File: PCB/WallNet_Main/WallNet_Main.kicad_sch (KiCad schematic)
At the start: 27 parts, among them J1 Conn_01x05_Pin, J2 USB_C_Receptacle_PowerOnly_6P, J3 Conn_01x04_Pin, J4 Conn_01x04_Pin, SW1 SW, SW2 SW, U1 NRF52810-QCAA-R7, U2 CPT-9019B-SMT-TR, U3 BQ25895RTWT, Y1 ECS-320-8-37CKM

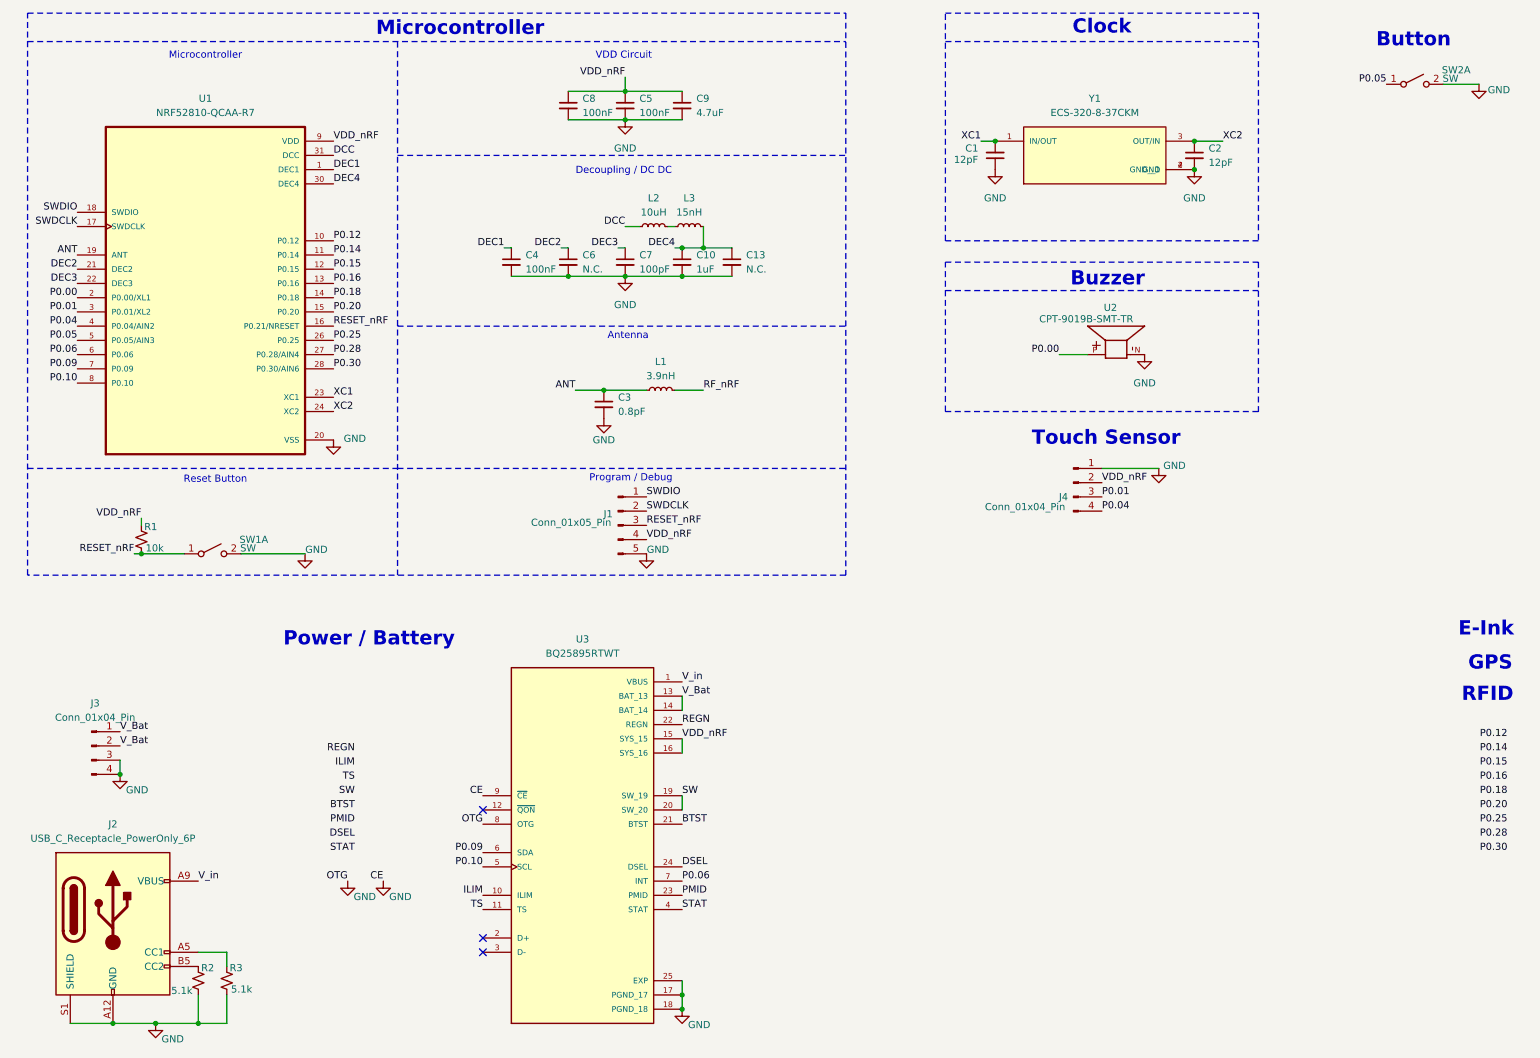
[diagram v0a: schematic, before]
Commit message: Changed Microcontroller
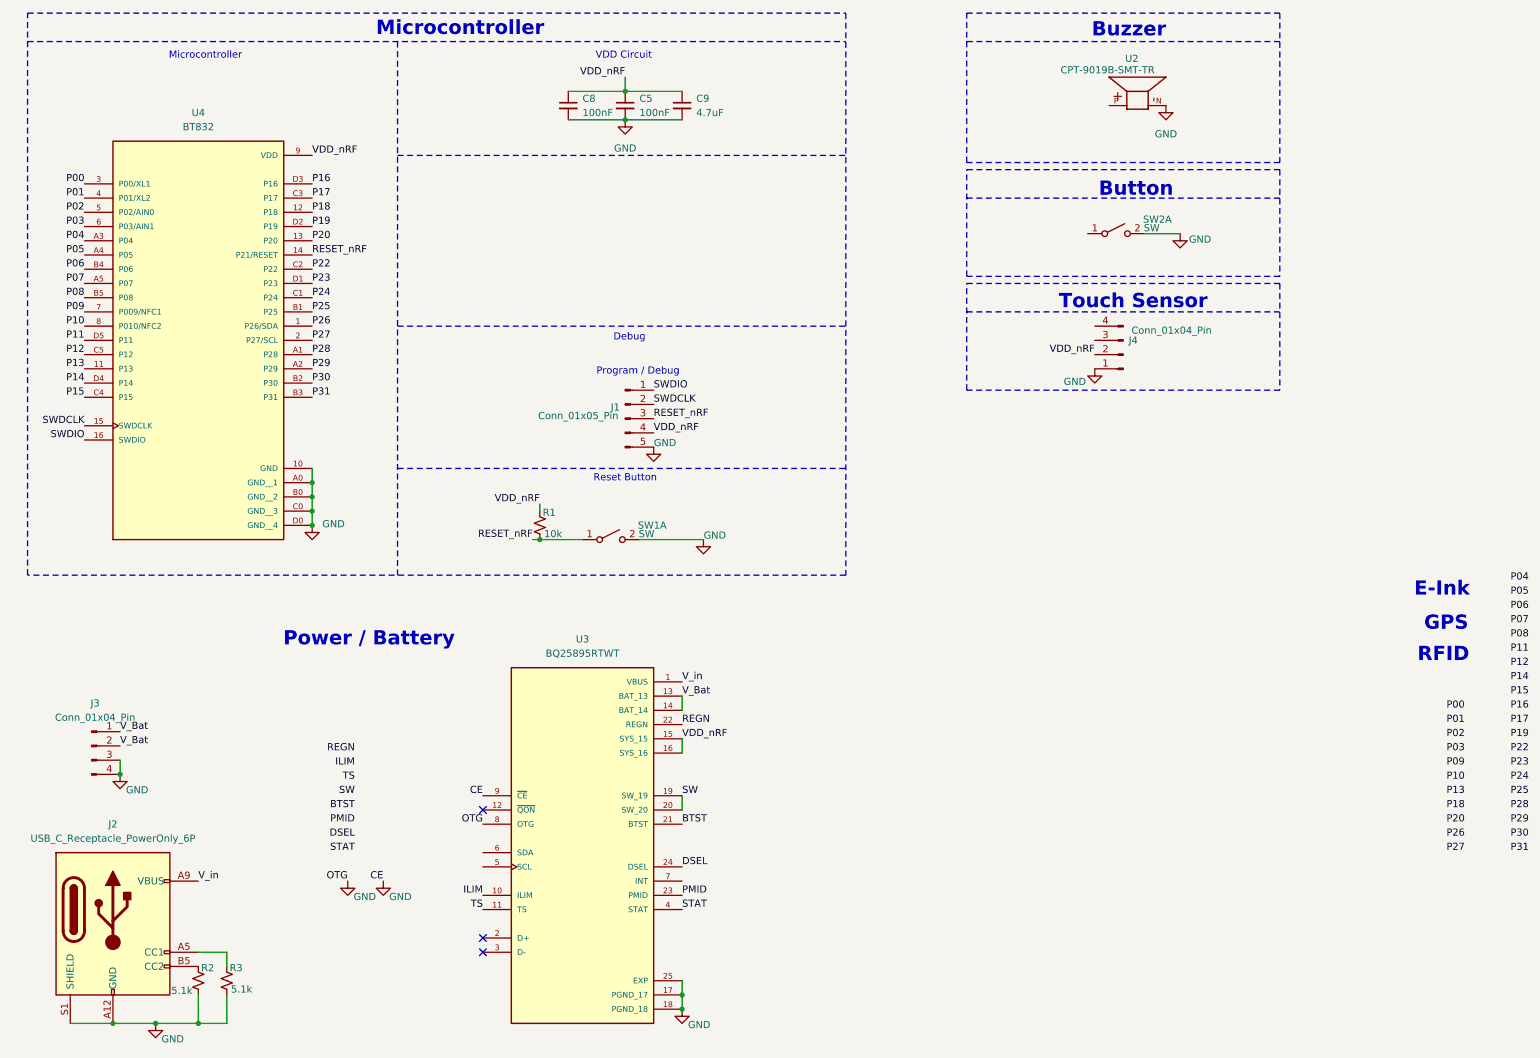
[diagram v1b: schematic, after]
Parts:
- removed C1, C2: 12pF, Capacitor_SMD:C_0402_1005Metric, symbol Device:C_Small
- removed C10: 1uF, Capacitor_SMD:C_0201_0603Metric, symbol Device:C_Small
- removed C13, C6: N.C., Capacitor_SMD:C_0402_1005Metric, symbol Device:C_Small
- removed C3: 0.8pF, Capacitor_SMD:C_0402_1005Metric, symbol Device:C_Small
- removed C4: 100nF, Capacitor_SMD:C_0402_1005Metric, symbol Device:C_Small
- removed C7: 100pF, Capacitor_SMD:C_0402_1005Metric, symbol Device:C_Small
- removed L1: 3.9nH, Inductor_SMD:L_0402_1005Metric, symbol Device:L_Small
- removed L2: 10uH, Inductor_SMD:L_0201_0603Metric, symbol Device:L_Small
- removed L3: 15nH, Inductor_SMD:L_0402_1005Metric, symbol Device:L_Small
- removed U1: NRF52810-QCAA-R7, NRF52810-QCAA-R7:QFN50P500X500X90-33N, symbol NRF52810-QCAA-R7:NRF52810-QCAA-R7
- removed Y1: ECS-320-8-37CKM, ECS_320_8_37CKM:XTAL_ECS-320-8-37CKM, symbol ECS-320-8-37CKM:ECS-320-8-37CKM
- added U4: BT832, BT832:BLEMODULE_BT832, symbol BT832:BT832
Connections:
- net GND: now also U4.10 (GND), U4.A0 (GND__1), U4.B0 (GND__2), U4.C0 (GND__3), U4.D0 (GND__4)
- net RESET_nRF: now also U4.14 (P21/RESET)
- net SWDCLK: now also U4.15 (SWDCLK)
- net SWDIO: now also U4.16 (SWDIO)
- net P0.00: no longer names the net of U2.P
- net P0.01: no longer names the net of J4.3 (Pin_3)
- net P0.04: no longer names the net of J4.4 (Pin_4)
- net P0.05: no longer names the net of SW2.1 (A)
- net P0.06: no longer names the net of U3.7 (INT)
- net P0.09: no longer names the net of U3.6 (SDA)
- net P0.10: no longer names the net of U3.5 (SCL)
- net VDD renamed VDD_nRF
- net VDD_nRF: now also U4.9 (VDD)
- new net P00: U4.3 (P00/XL1)
- new net P01: U4.4 (P01/XL2)
- new net P02: U4.5 (P02/AIN0)
- new net P03: U4.6 (P03/AIN1)
- new net P04: U4.A3 (P04)
- new net P05: U4.A4 (P05)
- new net P06: U4.B4 (P06)
- new net P07: U4.A5 (P07)
- new net P08: U4.B5 (P08)
- new net P09: U4.7 (P009/NFC1)
- new net P10: U4.8 (P010/NFC2)
- new net P11: U4.D5 (P11)
- new net P12: U4.C5 (P12)
- new net P13: U4.11 (P13)
- new net P14: U4.D4 (P14)
- new net P15: U4.C4 (P15)
- new net P16: U4.D3 (P16)
- new net P17: U4.C3 (P17)
- new net P18: U4.12 (P18)
- new net P19: U4.D2 (P19)
- new net P20: U4.13 (P20)
- new net P22: U4.C2 (P22)
- new net P23: U4.D1 (P23)
- new net P24: U4.C1 (P24)
- new net P25: U4.B1 (P25)
- new net P26: U4.1 (P26/SDA)
- new net P27: U4.2 (P27/SCL)
- new net P28: U4.A1 (P28)
- new net P29: U4.A2 (P29)
- new net P30: U4.B2 (P30)
- new net P31: U4.B3 (P31)
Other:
- note added: "Debug"
- note removed: "Antenna"
- note removed: "Clock"
- note removed: "Decoupling / DC DC"
- moved on the sheet: J1, J4, R1, SW1A, SW2A, U2

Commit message: Power Management Finished
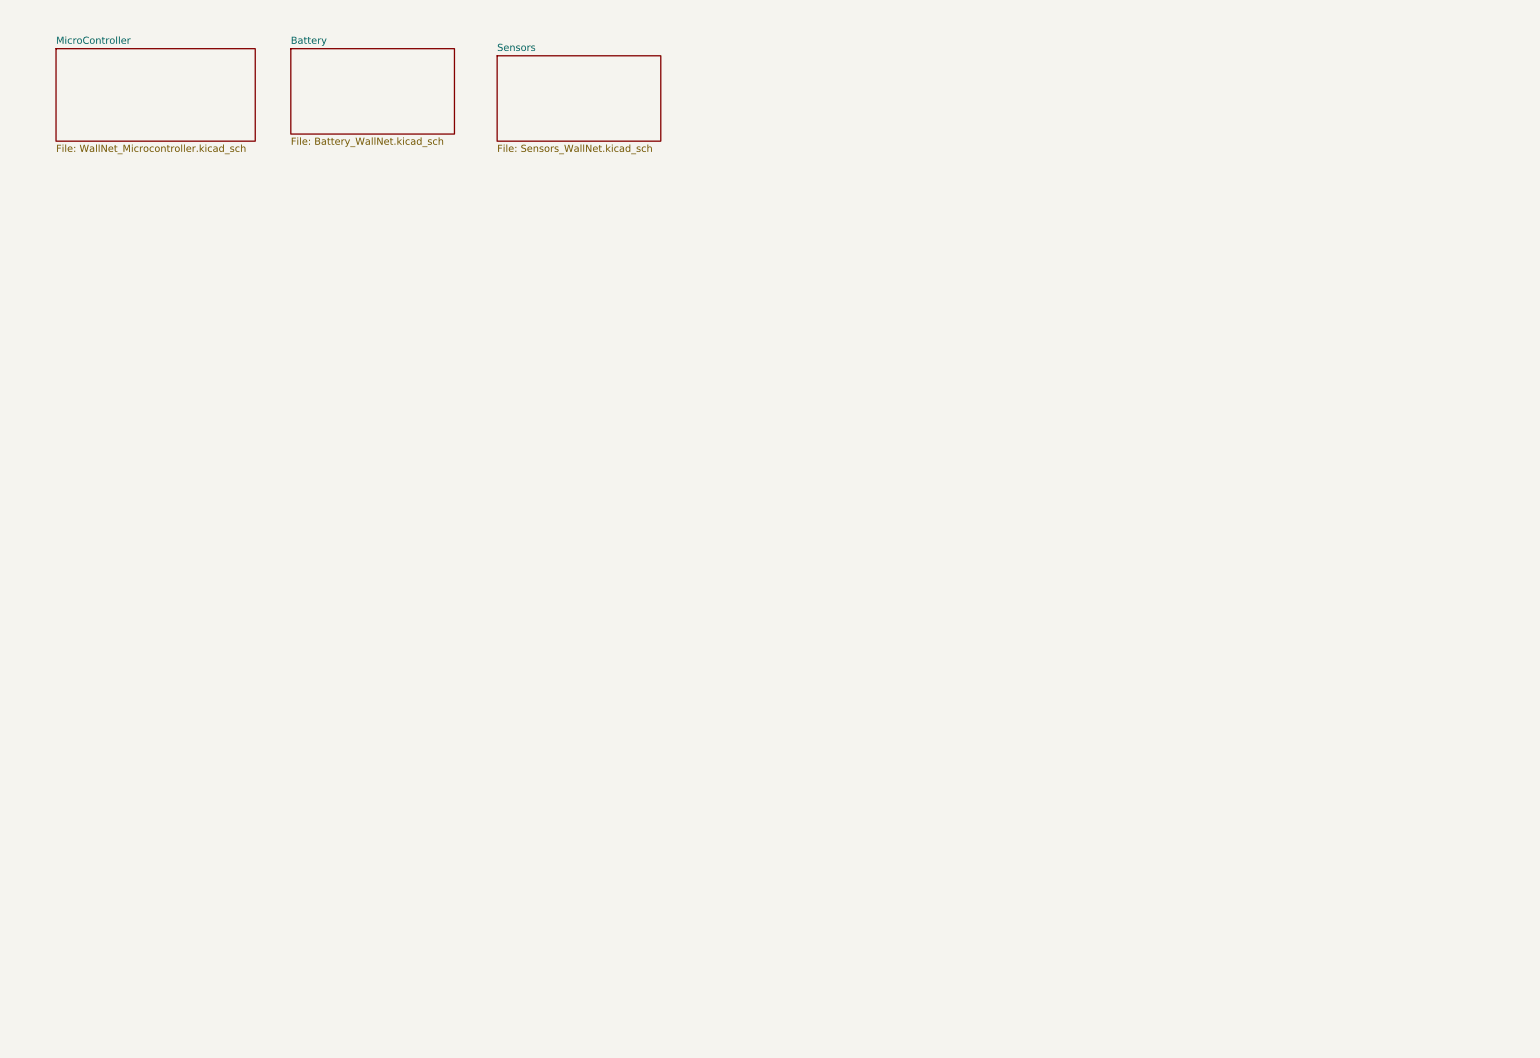
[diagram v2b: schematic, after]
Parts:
- removed C5, C8: 100nF, Capacitor_SMD:C_0402_1005Metric, symbol Device:C_Small
- removed C9: 4.7uF, Capacitor_SMD:C_0201_0603Metric, symbol Device:C_Small
- removed J1: Conn_01x05_Pin, Connector_PinHeader_2.54mm:PinHeader_1x05_P2.54mm_Vertical, symbol Connector:Conn_01x05_Pin
- removed J2: USB_C_Receptacle_PowerOnly_6P, symbol Connector:USB_C_Receptacle_PowerOnly_6P
- removed J3, J4: Conn_01x04_Pin, Connector_Molex:Molex_CLIK-Mate_502494-0470_1x04-1MP_P2.00mm_Horizontal, symbol Connector:Conn_01x04_Pin
- removed R1: 10k, Resistor_SMD:R_0201_0603Metric, symbol Device:R_Small_US
- removed R2, R3: 5.1k, Resistor_SMD:R_0201_0603Metric, symbol Device:R_Small_US
- removed SW1, SW2: SW, symbol Switch:SW_DPST_x2
- removed U2: CPT-9019B-SMT-TR, CPT_9019B_SMT_TR:XDCR_CPT-9019B-SMT-TR, symbol CPT-9019B-SMT-TR:CPT-9019B-SMT-TR
- removed U3: BQ25895RTWT, Package_DFN_QFN:Texas_RTW_WQFN-24-1EP_4x4mm_P0.5mm_EP2.7x2.7mm, symbol BQ25895RTWT:BQ25895RTWT
- removed U4: BT832, BT832:BLEMODULE_BT832, symbol BT832:BT832
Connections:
- no-connect marks 3 -> 0
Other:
- added sheet Battery (Battery_WallNet.kicad_sch)
- added sheet MicroController (WallNet_Microcontroller.kicad_sch)
- added sheet Sensors (Sensors_WallNet.kicad_sch)
- note removed: "Button"
- note removed: "Buzzer"
- note removed: "Debug"
- note removed: "E-Ink"
- note removed: "GPS"
- note removed: "Microcontroller"
- note removed: "Power / Battery"
- note removed: "Program / Debug"
- note removed: "RFID"
- note removed: "Reset Button"
- note removed: "Touch Sensor"
- note removed: "VDD Circuit"

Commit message: bruh
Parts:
- added C1, C2: 100nF, Capacitor_SMD:C_0402_1005Metric, symbol Device:C_Small
- added C3: 4.7uF, Capacitor_SMD:C_0201_0603Metric, symbol Device:C_Small
- added J1: Conn_01x05_Pin, Connector_PinHeader_2.54mm:PinHeader_1x05_P2.54mm_Vertical, symbol Connector:Conn_01x05_Pin
- added R1: 10k, symbol Device:R_Small_US
- added SW1: SW, symbol Switch:SW_DPST_x2
- added U4: BT832, BT832:BLEMODULE_BT832, symbol BT832:BT832
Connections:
- new net GND: C1.2, C2.2, C3.2, J1.5 (Pin_5), SW1.2 (B), U4.10 (GND), U4.A0 (GND__1), U4.B0 (GND__2), U4.C0 (GND__3), U4.D0 (GND__4)
- new net P00: U4.3 (P00/XL1)
- new net P01: U4.4 (P01/XL2)
- new net P02: U4.5 (P02/AIN0)
- new net P03: U4.6 (P03/AIN1)
- new net P04: U4.A3 (P04)
- new net P05: U4.A4 (P05)
- new net P06: U4.B4 (P06)
- new net P07: U4.A5 (P07)
- new net P08: U4.B5 (P08)
- new net P09: U4.7 (P009/NFC1)
- new net P10: U4.8 (P010/NFC2)
- new net P11: U4.D5 (P11)
- new net P12: U4.C5 (P12)
- new net P13: U4.11 (P13)
- new net P14: U4.D4 (P14)
- new net P15: U4.C4 (P15)
- new net P16: U4.D3 (P16)
- new net P17: U4.C3 (P17)
- new net P18: U4.12 (P18)
- new net P19: U4.D2 (P19)
- new net P20: U4.13 (P20)
- new net P22: U4.C2 (P22)
- new net P23: U4.D1 (P23)
- new net P24: U4.C1 (P24)
- new net P25: U4.B1 (P25)
- new net P26: U4.1 (P26/SDA)
- new net P27: U4.2 (P27/SCL)
- new net P28: U4.A1 (P28)
- new net P29: U4.A2 (P29)
- new net P30: U4.B2 (P30)
- new net P31: U4.B3 (P31)
- new net RESET_nRF: J1.3 (Pin_3), R1.2, SW1.1 (A), U4.14 (P21/RESET)
- new net SWDCLK: J1.2 (Pin_2), U4.15 (SWDCLK)
- new net SWDIO: J1.1 (Pin_1), U4.16 (SWDIO)
- new net VDD_nRF: C1.1, C2.1, C3.1, J1.4 (Pin_4)
- new net VDD_nrf: R1.1, U4.9 (VDD)
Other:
- removed sheet MicroController
- sheet Battery ports: added BQ_INT, BQ_SCL, BQ_SDA; removed none
- note added: "Debug"
- note added: "Microcontroller"
- note added: "Program / Debug"
- note added: "Reset Button"
- note added: "VDD Circuit"

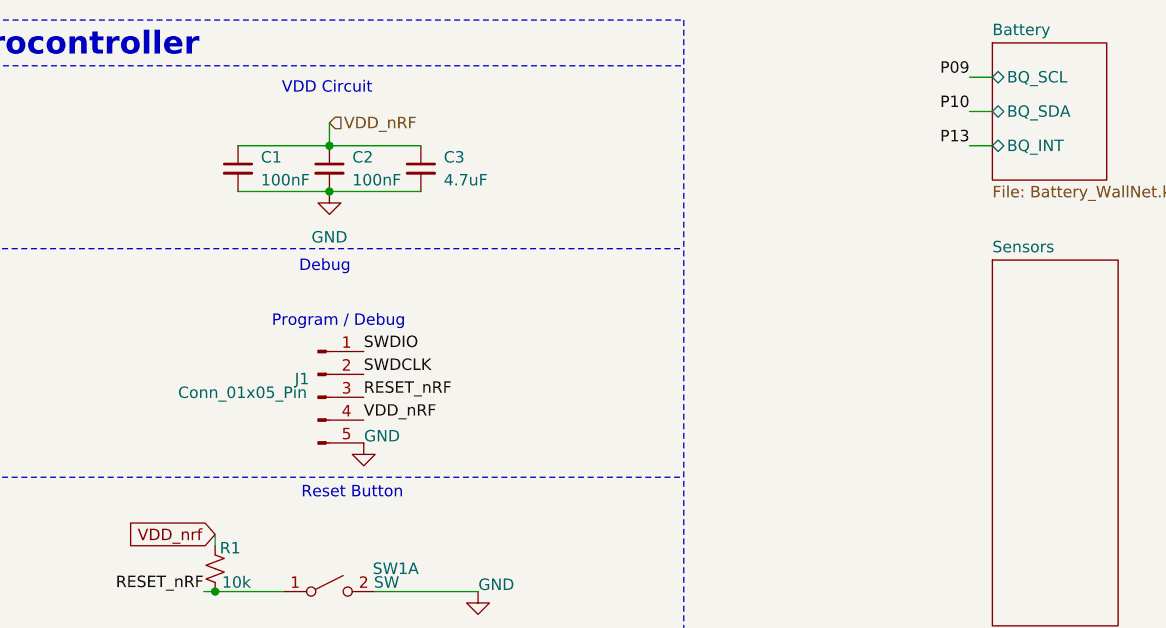
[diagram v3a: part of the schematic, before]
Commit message: Changed some Heir connections
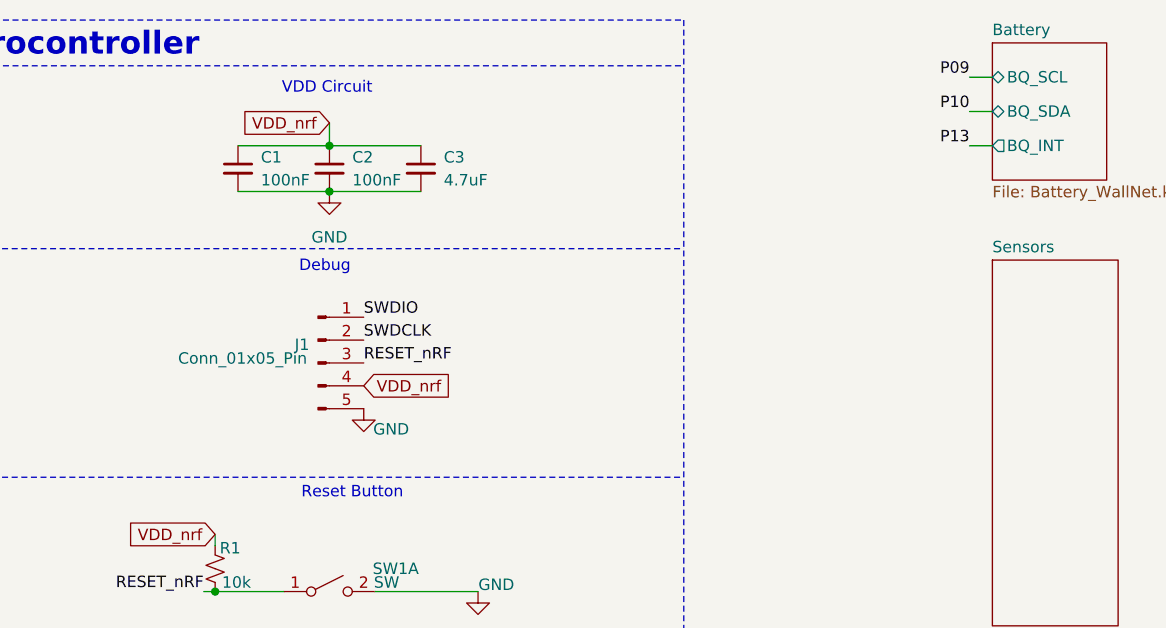
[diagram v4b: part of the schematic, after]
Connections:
- net VDD_nRF is gone; now on net VDD_nrf: C1.1, C2.1, C3.1, J1.4 (Pin_4)
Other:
- note removed: "Program / Debug"
- moved on the sheet: J1
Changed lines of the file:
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@@
-		)
-	)
-	(text "Program / Debug"
-		(exclude_from_sim no)
-		(at 125.476 56.388 0)
-		(effects
-			(font
-				(size 1.27 1.27)
-			)
 		)
 	)
@@
 	)
 	(label "SWDCLK"
-		(at 128.27 62.23 0)
+		(at 128.27 58.42 0)
 		(effects
 			(font
@@
 		)
 	)
-	(label "VDD_nRF"
-		(at 128.27 67.31 0)
-		(effects
-			(font
-				(size 1.27 1.27)
-			)
-			(justify left bottom)
-		)
-	)
 	(label "P16"
 		(at 68.58 53.34 0)
@@
 	)
 	(label "RESET_nRF"
-		(at 128.27 64.77 0)
+		(at 128.27 60.96 0)
 		(effects
 			(font
@@
 	)
 	(label "SWDIO"
-		(at 128.27 59.69 0)
+		(at 128.27 55.88 0)
 		(effects
 			(font
@@
 			)
 			(justify left bottom)
+		)
+	)
+	(global_label "VDD_nrf"
+		(shape input)
+		(at 128.27 63.5 0)
+		(fields_autoplaced yes)
+		(effects
+			(font
+				(size 1.27 1.27)
+			)
+			(justify left)
+		)
+		(property "Intersheetrefs" "${INTERSHEET_REFS}"
+			(at 138.5123 63.5 0)
+			(effects
+				(font
+					(size 1.27 1.27)
+				)
+				(justify left)
+				(hide yes)
+			)
+		)
+	)
+	(global_label "VDD_nrf"
+		(shape input)
+		(at 124.46 34.29 180)
+		(fields_autoplaced yes)
+		(effects
+			(font
+				(size 1.27 1.27)
+			)
+			(justify right)
+		)
+		(property "Intersheetrefs" "${INTERSHEET_REFS}"
+			(at 114.2177 34.29 0)
+			(effects
+				(font
+					(size 1.27 1.27)
+				)
+				(justify right)
+				(hide yes)
+			)
 		)
 	)
@@
 		)
 	)
-	(hierarchical_label "VDD_nRF"
-		(shape input)
-		(at 124.46 34.29 0)
-		(effects
-			(font
-				(size 1.27 1.27)
-			)
-			(justify left)
-		)
-	)
 	(symbol
 		(lib_id "Connector:Conn_01x05_Pin")
-		(at 123.19 64.77 0)
+		(at 123.19 60.96 0)
 		(unit 1)
 		(exclude_from_sim no)
@@
 		(dnp no)
 		(property "Reference" "J1"
-			(at 121.412 62.738 0)
+			(at 121.412 58.928 0)
 			(effects
 				(font
@@
 		)
 		(property "Value" "Conn_01x05_Pin"
-			(at 114.808 64.262 0)
+			(at 114.808 60.452 0)
 			(effects
 				(font
@@
 		)
 		(property "Footprint" "Connector_PinHeader_2.54mm:PinHeader_1x05_P2.54mm_Vertical"
-			(at 123.19 64.77 0)
+			(at 123.19 60.96 0)
 			(effects
 				(font
@@
 		)
 		(property "Datasheet" "~"
-			(at 123.19 64.77 0)
+			(at 123.19 60.96 0)
 			(effects
 				(font
@@
 		)
 		(property "Description" "Generic connector, single row, 01x05, script generated"
-			(at 123.19 64.77 0)
+			(at 123.19 60.96 0)
 			(effects
 				(font
@@
 	(symbol
 		(lib_id "power:GND")
-		(at 128.27 69.85 0)
+		(at 128.27 66.04 0)
 		(unit 1)
 		(exclude_from_sim no)
@@
 		(dnp no)
 		(property "Reference" "#PWR08"
-			(at 128.27 76.2 0)
+			(at 128.27 72.39 0)
 			(effects
 				(font
@@
 		)
 		(property "Value" "GND"
-			(at 130.302 69.088 0)
+			(at 131.318 68.326 0)
 			(effects
 				(font
@@
 		)
 		(property "Footprint" ""
-			(at 128.27 69.85 0)
+			(at 128.27 66.04 0)
 			(effects
 				(font
@@
 		)
 		(property "Datasheet" ""
-			(at 128.27 69.85 0)
+			(at 128.27 66.04 0)
 			(effects
 				(font
@@
 		)
 		(property "Description" "Power symbol creates a global label with name \"GND\" , ground"
-			(at 128.27 69.85 0)
+			(at 128.27 66.04 0)
 			(effects
 				(font
@@
 			)
 		)
-		(pin "BQ_INT" bidirectional
+		(pin "BQ_INT" output
 			(at 198.12 36.83 180)
 			(effects
